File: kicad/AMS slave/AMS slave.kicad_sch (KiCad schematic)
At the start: 45 parts

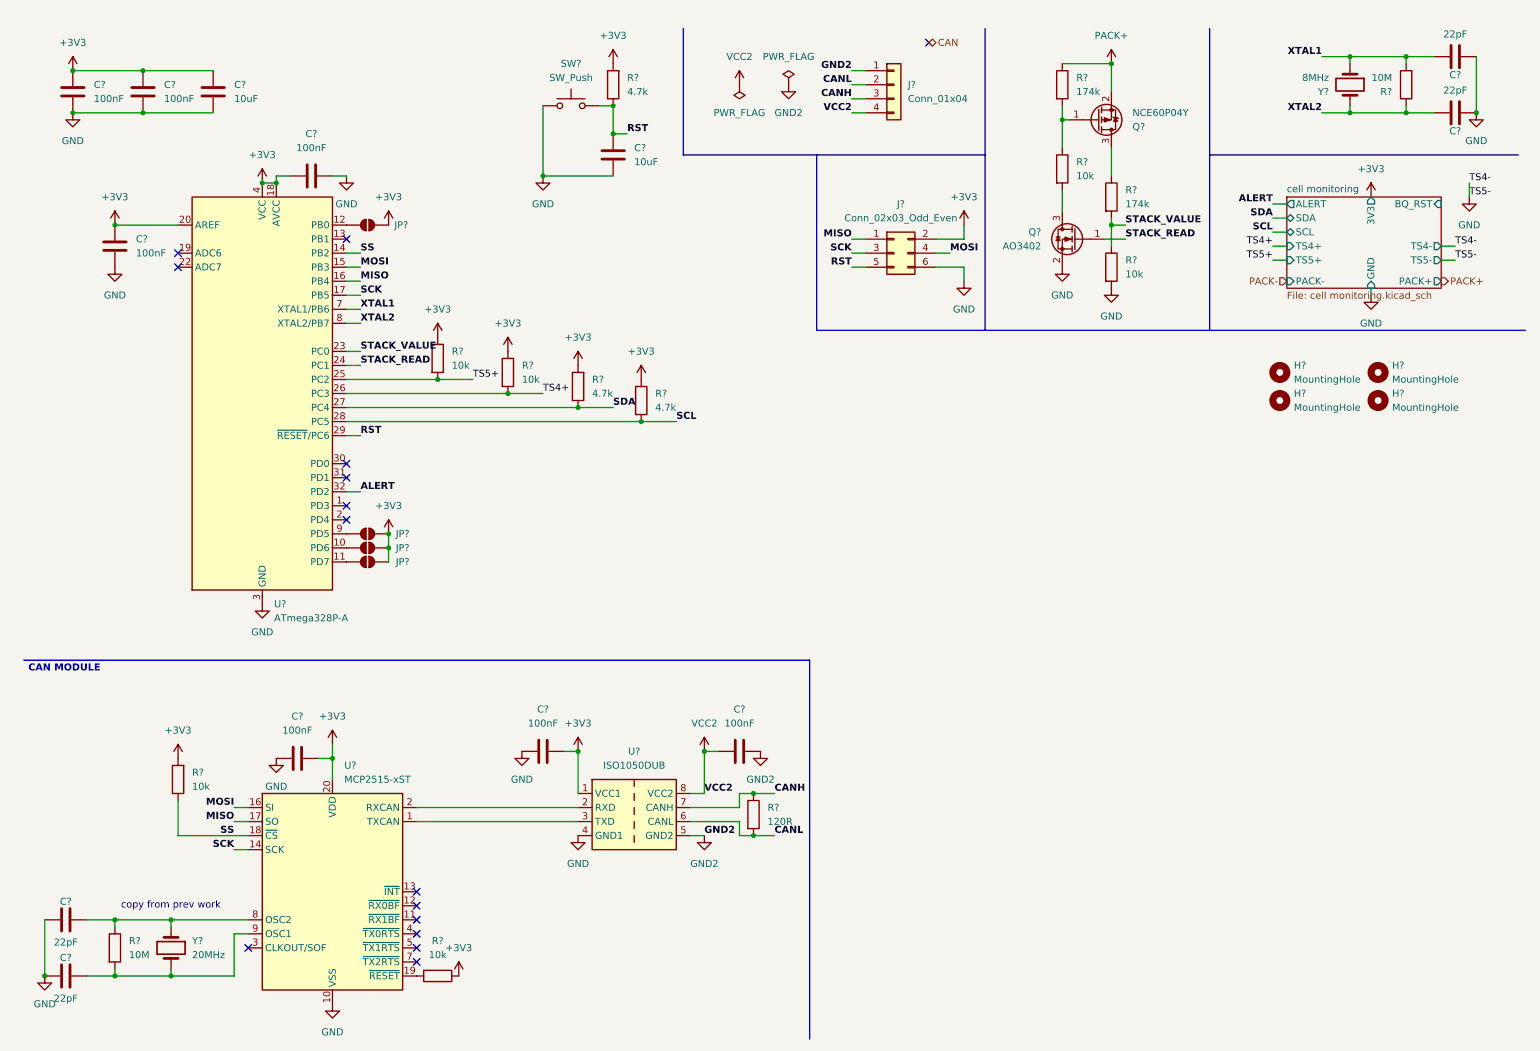
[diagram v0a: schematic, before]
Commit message: AMS slave schem 0.4.3, pcb 0.4.4
schematic: switched out thermistors for 1x02 MP connector symbols, fixed mangled annotations
PCB: switched out thermistor connectors for the correct type
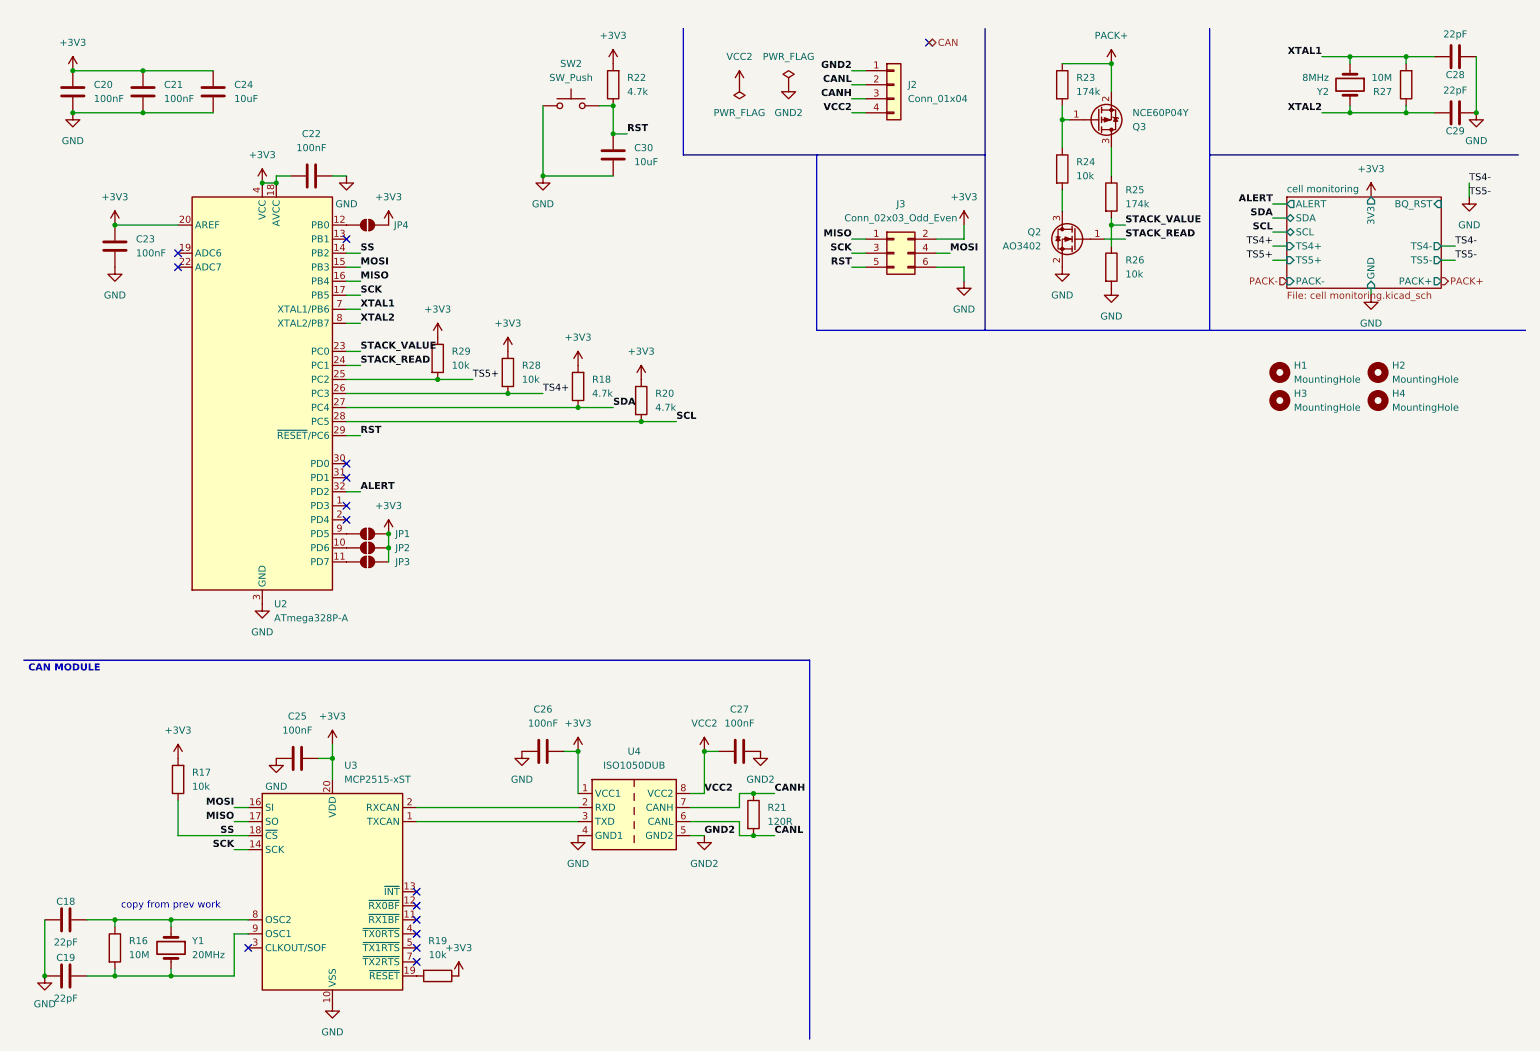
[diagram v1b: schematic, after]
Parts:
- gave numbers to parts that had none: 45
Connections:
- net +3V3: now also C22.1, C23.2; no longer C22.2, C23.1
- net GND: now also C22.2, C23.1; no longer C22.1, C23.2
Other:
- moved on the sheet: C22, C23

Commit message: AMS slave schem 0.4.4 pcb 0.5.0
schematic cleaned up with labels and removed clipping text
new PCB iteration, with generally shorter traces where applicable, better filter capacitor layout, and pinout labels with silkscreen
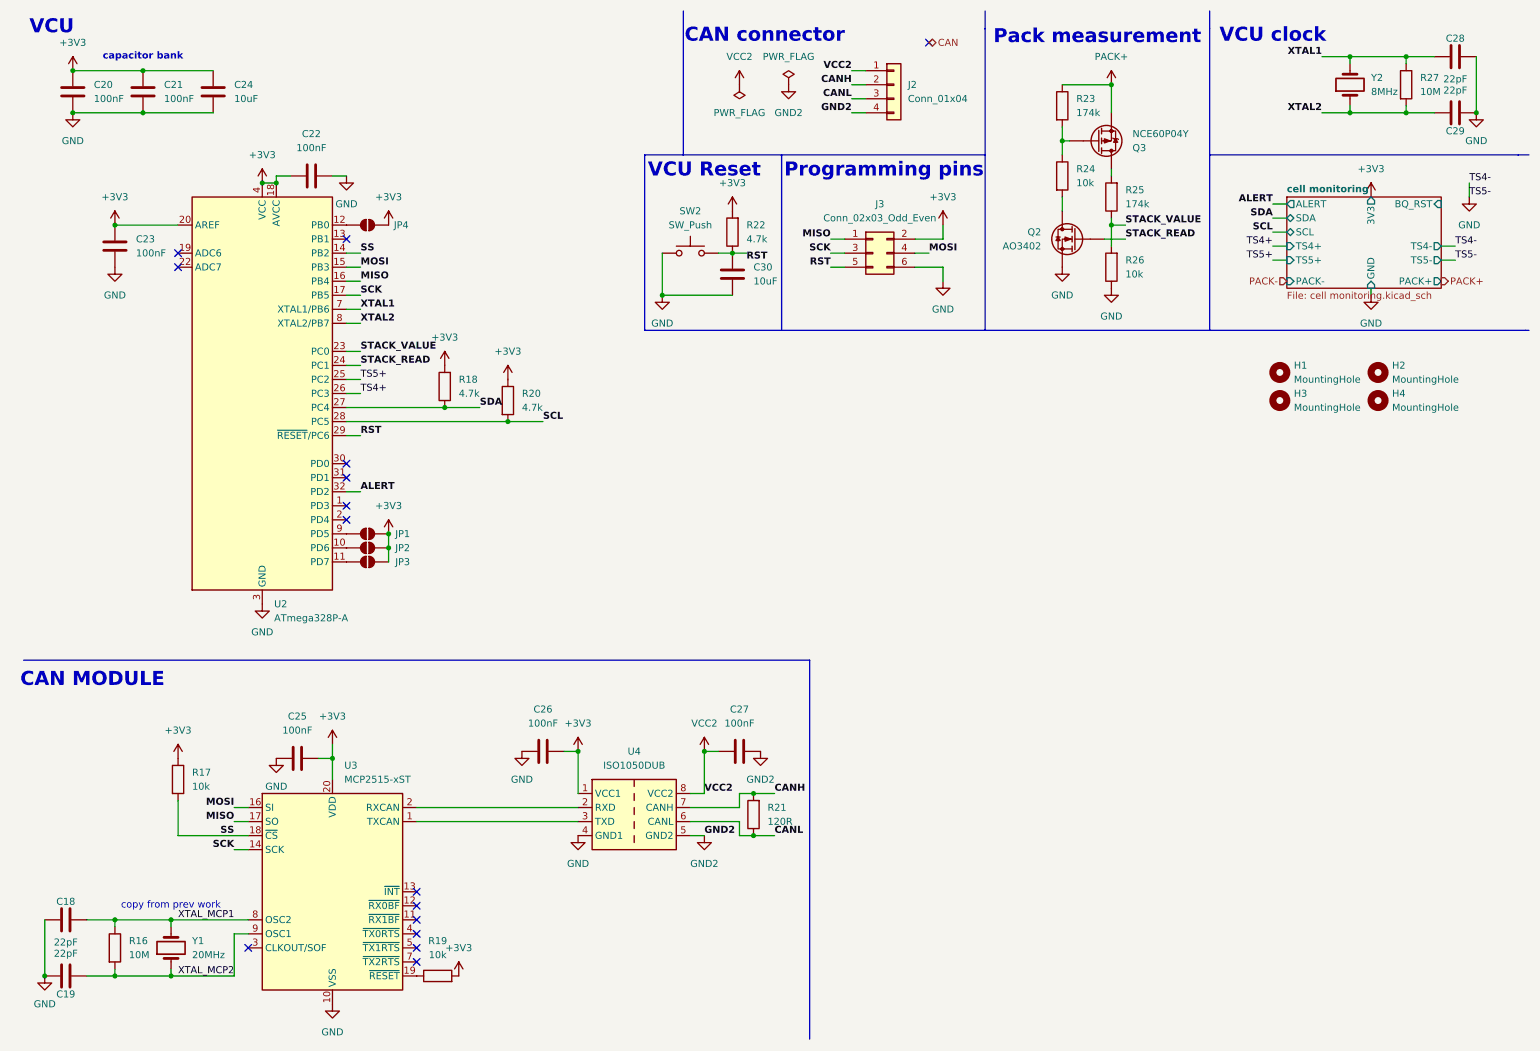
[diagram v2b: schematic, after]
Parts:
- removed R28, R29: 10k, RMC_Resistor:R_0805_2012Metric_Pad1.20x1.40mm_HandSolder_L, symbol Device:R
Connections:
- net +3V3: now also R17.1, R19.2; no longer R17.2, R19.1
- net CANH: now also J2.2 (Pin_2), R21.2; no longer J2.3 (Pin_3), R21.1
- net CANL: now also J2.3 (Pin_3), R21.1; no longer J2.2 (Pin_2), R21.2
- net GND: now also C19.2, C29.2, R26.1; no longer C19.1, C29.1, R26.2
- net GND2: now also J2.4 (Pin_4); no longer J2.1 (Pin_1)
- net SS: now also R17.2; no longer R17.1
- net STACK_VALUE: now also R25.1, R26.2; no longer R25.2, R26.1
- net VCC2: now also J2.1 (Pin_1); no longer J2.4 (Pin_4)
- net XTAL1: now also R27.1, Y2.2; no longer R27.2, Y2.1
- net XTAL2: now also C29.1, R27.2, Y2.1; no longer C29.2, R27.1, Y2.2
- net at U3.19 (~{RESET}): now also R19.1; no longer R19.2
- net XTAL_MCP1: now reaches C18.2, R16.1, U3.8 (OSC2)
- net XTAL_MCP1: now also Y1.2; no longer Y1.1
- net XTAL_MCP2: now reaches R16.2, U3.9 (OSC1)
- net XTAL_MCP2: now also C19.1, Y1.1; no longer C19.2, Y1.2
- net at Q3.3 (D): now also R25.2; no longer R25.1
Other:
- note added: "CAN connector"
- note added: "Pack measurement"
- note added: "Programming pins"
- note added: "VCU"
- note added: "VCU Reset"
- note added: "VCU clock"
- note added: "capacitor bank"
- title: (none) -> AMS slave control
- moved on the sheet: C19, C29, C30, J3, R17, R18, R19, R20, R21, R22, R23, R24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

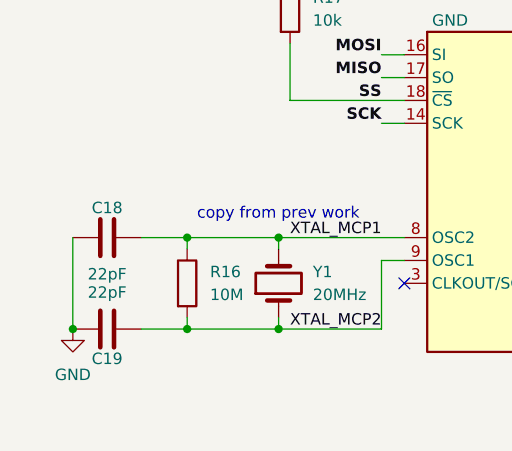
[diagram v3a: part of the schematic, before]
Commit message: Schem 0.4.6
Changed 20MHz crystal capacitor values.
BOM updated
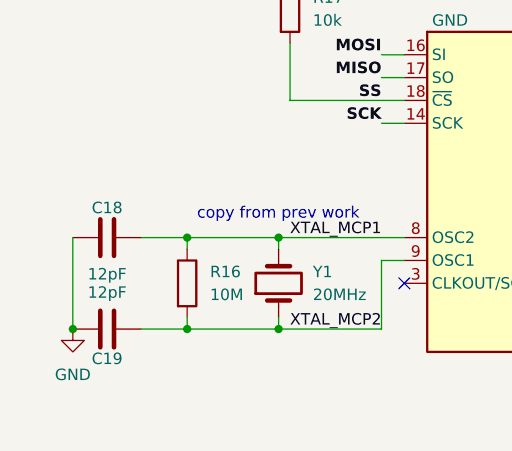
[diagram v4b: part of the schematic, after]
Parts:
- C18, C19: value 22pF -> 12pF
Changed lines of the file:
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@@
 		(title "AMS slave control")
 		(date "2026-03-05")
-		(rev "0.4.5")
+		(rev "0.4.6")
 	)
 	(text "Programming pins"
@@
 			)
 		)
-		(property "Value" "22pF"
+		(property "Value" "12pF"
 			(at 20.32 182.626 90)
 			(effects
@@
 			)
 		)
-		(property "Value" "22pF"
+		(property "Value" "12pF"
 			(at 20.32 180.594 90)
 			(effects
